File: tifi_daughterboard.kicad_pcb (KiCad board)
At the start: 2 copper layers, 57.4 x 32.3 mm, 19 parts, among them J1 SSW-110-23-F-D, J2 SSW-110-23-F-D, J3 SM04B-SRSS-TB(LF)(SN), J4 SSW-103-02-T-S-RA, Q1 BSS138LT1G, U1 SGP40-D-R4, U2 SHT40-AD1B-R3

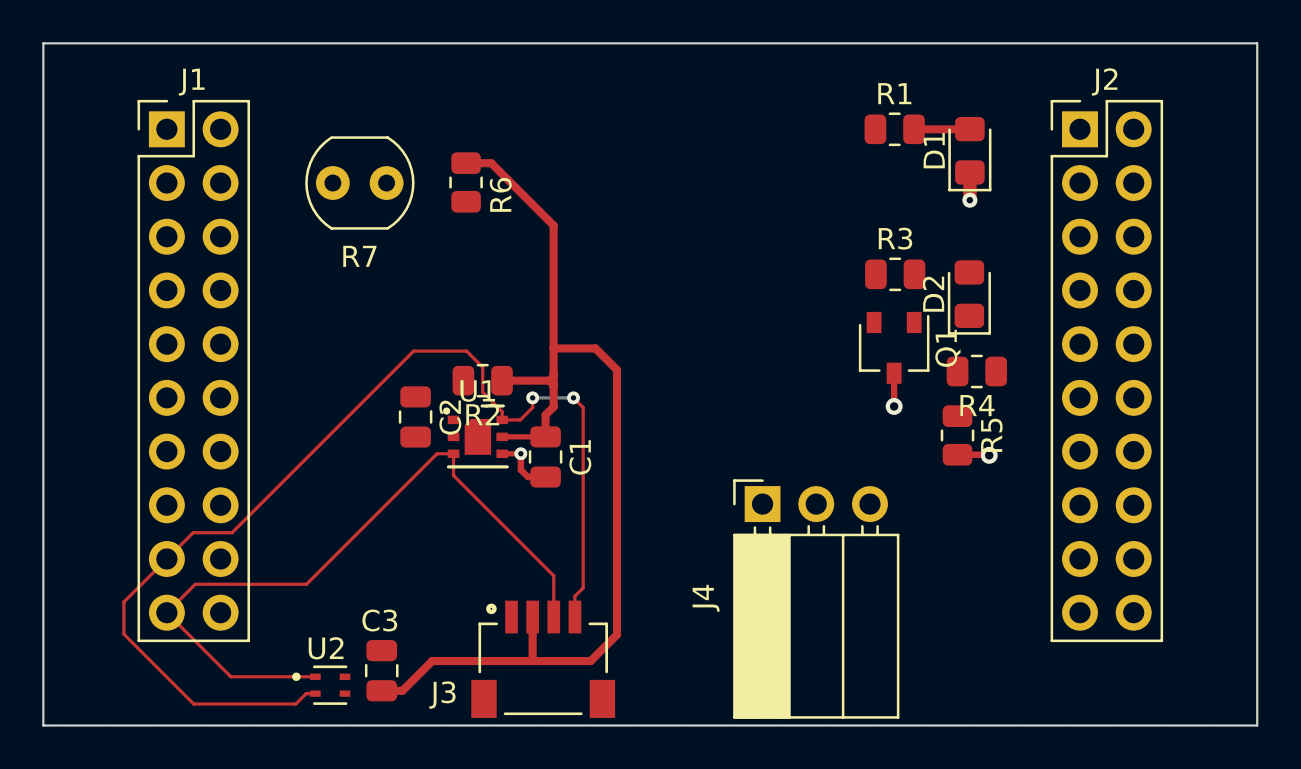
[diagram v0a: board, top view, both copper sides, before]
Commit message: Route 5V rail
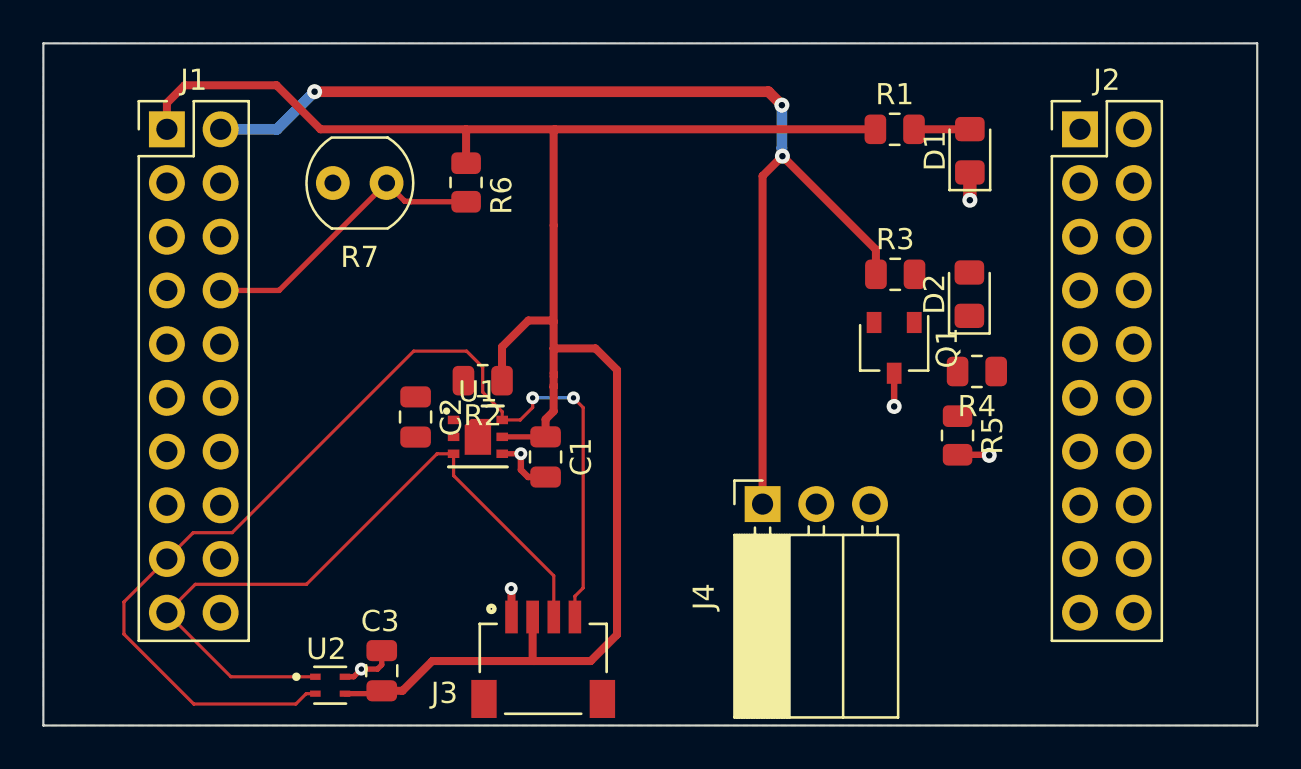
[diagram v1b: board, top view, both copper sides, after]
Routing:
- net +5V: track 0.00 -> 54.2 mm, vias 0 -> 3
- net +3.3V: track 51.0 -> 91.1 mm
- net LDR_OUT: track 0.00 -> 14.1 mm
- net GND: track 7.35 -> 11.3 mm, vias 4 -> 6
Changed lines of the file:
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@@
   (gr_rect (start 116.078 69.596) (end 173.482 101.854) (layer "Edge.Cuts") (width 0.1016) (fill none))
   (segment (start 139.2682 98.806) (end 134.4676 98.806) (width 0.381) (layer "F.Cu") (net 1))
+  (segment (start 140.208 85.852) (end 140.208 86.995) (width 0.381) (layer "F.Cu") (net 1))
+  (segment (start 129.1844 73.66) (end 136.0678 73.66) (width 0.381) (layer "F.Cu") (net 1))
+  (segment (start 137.7677 85.5472) (end 137.7677 83.9489) (width 0.381) (layer "F.Cu") (net 1))
+  (segment (start 140.208 78.2066) (end 140.208 82.7532) (width 0.381) (layer "F.Cu") (net 1))
   (segment (start 141.9606 98.806) (end 139.2682 98.806) (width 0.381) (layer "F.Cu") (net 1))
+  (segment (start 140.208 73.7108) (end 140.2588 73.66) (width 0.381) (layer "F.Cu") (net 1))
+  (segment (start 139.827 87.376) (end 139.827 88.204) (width 0.381) (layer "F.Cu") (net 1))
   (segment (start 139.2682 98.806) (end 139.215 98.7528) (width 0.381) (layer "F.Cu") (net 1))
-  (segment (start 136.0678 75.2621) (end 137.2635 75.2621) (width 0.381) (layer "F.Cu") (net 1))
+  (segment (start 136.0678 75.2621) (end 136.0678 73.66) (width 0.381) (layer "F.Cu") (net 1))
   (segment (start 139.215 98.7528) (end 139.215 96.7232) (width 0.381) (layer "F.Cu") (net 1))
+  (segment (start 139.0142 82.7024) (end 140.1572 82.7024) (width 0.381) (layer "F.Cu") (net 1))
+  (segment (start 136.0678 73.66) (end 140.2588 73.66) (width 0.381) (layer "F.Cu") (net 1))
   (segment (start 143.2052 97.5614) (end 141.9606 98.806) (width 0.381) (layer "F.Cu") (net 1))
   (segment (start 133.0604 100.2132) (end 132.08 100.2132) (width 0.381) (layer "F.Cu") (net 1))
-  (segment (start 140.208 78.2066) (end 140.208 84.0232) (width 0.381) (layer "F.Cu") (net 1))
-  (segment (start 140.208 86.7918) (end 139.827 87.1728) (width 0.381) (layer "F.Cu") (net 1))
+  (segment (start 121.92 72.4154) (end 122.7582 71.5772) (width 0.381) (layer "F.Cu") (net 1))
+  (segment (start 140.2588 73.66) (end 155.4245 73.66) (width 0.381) (layer "F.Cu") (net 1))
   (segment (start 140.208 84.0232) (end 142.1892 84.0232) (width 0.381) (layer "F.Cu") (net 1))
   (segment (start 140.208 85.852) (end 140.208 85.7504) (width 0.381) (layer "F.Cu") (net 1))
-  (segment (start 139.827 87.1728) (end 139.827 88.204) (width 0.381) (layer "F.Cu") (net 1))
+  (segment (start 127.1016 71.5772) (end 129.1844 73.66) (width 0.381) (layer "F.Cu") (net 1))
+  (segment (start 131.9442 100.349) (end 132.08 100.2132) (width 0.254) (layer "F.Cu") (net 1))
   (segment (start 142.1892 84.0232) (end 143.2052 85.0392) (width 0.381) (layer "F.Cu") (net 1))
+  (segment (start 137.7677 83.9489) (end 139.0142 82.7024) (width 0.381) (layer "F.Cu") (net 1))
   (segment (start 140.208 85.344) (end 140.208 85.852) (width 0.381) (layer "F.Cu") (net 1))
   (segment (start 140.208 85.1916) (end 140.208 85.344) (width 0.381) (layer "F.Cu") (net 1))
-  (segment (start 137.2635 75.2621) (end 140.208 78.2066) (width 0.381) (layer "F.Cu") (net 1))
   (segment (start 140.208 84.0232) (end 140.208 85.1916) (width 0.381) (layer "F.Cu") (net 1))
-  (segment (start 140.208 85.344) (end 140.0048 85.5472) (width 0.381) (layer "F.Cu") (net 1))
+  (segment (start 140.208 82.7532) (end 140.208 84.0232) (width 0.381) (layer "F.Cu") (net 1))
+  (segment (start 122.7582 71.5772) (end 127.1016 71.5772) (width 0.381) (layer "F.Cu") (net 1))
+  (segment (start 140.1572 82.7024) (end 140.208 82.7532) (width 0.381) (layer "F.Cu") (net 1))
   (segment (start 143.2052 85.0392) (end 143.2052 97.5614) (width 0.381) (layer "F.Cu") (net 1))
   (segment (start 137.7766 88.204) (end 139.827 88.204) (width 0.254) (layer "F.Cu") (net 1))
-  (segment (start 140.208 85.852) (end 140.208 86.7918) (width 0.381) (layer "F.Cu") (net 1))
-  (segment (start 137.5645 85.5472) (end 140.0048 85.5472) (width 0.381) (layer "F.Cu") (net 1))
+  (segment (start 130.3416 100.349) (end 131.9442 100.349) (width 0.254) (layer "F.Cu") (net 1))
+  (segment (start 140.208 78.2066) (end 140.208 73.7108) (width 0.381) (layer "F.Cu") (net 1))
+  (segment (start 140.208 86.995) (end 139.827 87.376) (width 0.381) (layer "F.Cu") (net 1))
   (segment (start 134.4676 98.806) (end 133.0604 100.2132) (width 0.381) (layer "F.Cu") (net 1))
-  (segment (start 140.208 85.7504) (end 140.0048 85.5472) (width 0.381) (layer "F.Cu") (net 1))
+  (segment (start 121.92 73.66) (end 121.92 72.4154) (width 0.381) (layer "F.Cu") (net 1))
+  (segment (start 138.215 95.4668) (end 138.215 96.7232) (width 0.381) (layer "F.Cu") (net 2))
   (segment (start 137.7766 89.004) (end 138.6562 89.004) (width 0.254) (layer "F.Cu") (net 2))
+  (segment (start 131.1148 99.187) (end 131.8768 99.187) (width 0.254) (layer "F.Cu") (net 2))
   (segment (start 138.6586 89.7636) (end 138.999 90.104) (width 0.3048) (layer "F.Cu") (net 2))
   (segment (start 159.893 77.0128) (end 159.893 75.701) (width 0.635) (layer "F.Cu") (net 2))
   (segment (start 159.3088 89.0505) (end 160.7801 89.0505) (width 0.3048) (layer "F.Cu") (net 2))
+  (segment (start 131.8768 99.187) (end 132.08 98.9838) (width 0.254) (layer "F.Cu") (net 2))
+  (segment (start 138.2014 95.4532) (end 138.215 95.4668) (width 0.381) (layer "F.Cu") (net 2))
   (segment (start 138.6562 89.004) (end 138.6586 89.0016) (width 0.254) (layer "F.Cu") (net 2))
+  (segment (start 130.7528 99.549) (end 131.1148 99.187) (width 0.254) (layer "F.Cu") (net 2))
+  (segment (start 130.3416 99.549) (end 130.7528 99.549) (width 0.254) (layer "F.Cu") (net 2))
   (segment (start 156.3116 85.1959) (end 156.3116 86.7664) (width 0.3048) (layer "F.Cu") (net 2))
   (segment (start 138.999 90.104) (end 139.827 90.104) (width 0.3048) (layer "F.Cu") (net 2))
   (segment (start 160.7801 89.0505) (end 160.8074 89.0778) (width 0.3048) (layer "F.Cu") (net 2))
   (segment (start 138.6586 89.0016) (end 138.6586 89.7636) (width 0.3048) (layer "F.Cu") (net 2))
-  (via (at 160.8074 89.0778) (size 0.8) (drill 0.4) (layers "F.Cu" "B.Cu") (net 2))
+  (segment (start 132.08 98.9838) (end 132.08 98.3132) (width 0.254) (layer "F.Cu") (net 2))
+  (via (at 131.1148 99.187) (size 0.6096) (drill 0.254) (layers "F.Cu" "B.Cu") (free) (net 2))
+  (via (at 160.8074 89.0778) (size 0.7112) (drill 0.3048) (layers "F.Cu" "B.Cu") (net 2))
+  (via (at 138.2014 95.377) (size 0.6096) (drill 0.254) (layers "F.Cu" "B.Cu") (free) (net 2))
   (via (at 138.6586 89.0016) (size 0.6096) (drill 0.254) (layers "F.Cu" "B.Cu") (net 2))
   (via (at 159.893 77.0128) (size 0.7112) (drill 0.3048) (layers "F.Cu" "B.Cu") (free) (net 2))
-  (via (at 156.3116 86.7664) (size 0.8) (drill 0.4) (layers "F.Cu" "B.Cu") (net 2))
+  (via (at 156.3116 86.7664) (size 0.7112) (drill 0.3048) (layers "F.Cu" "B.Cu") (net 2))
   (segment (start 157.2495 73.66) (end 159.884 73.66) (width 0.381) (layer "F.Cu") (net 3))
   (segment (start 159.884 73.66) (end 159.893 73.651) (width 0.381) (layer "F.Cu") (net 3))
+  (segment (start 151.0284 74.93) (end 150.0886 75.8698) (width 0.381) (layer "F.Cu") (net 6))
+  (segment (start 128.905 71.882) (end 150.368 71.882) (width 0.508) (layer "F.Cu") (net 6))
+  (segment (start 150.368 71.882) (end 151.003 72.517) (width 0.508) (layer "F.Cu") (net 6))
+  (segment (start 151.0284 74.93) (end 155.4499 79.3515) (width 0.381) (layer "F.Cu") (net 6))
+  (segment (start 150.0886 75.8698) (end 150.0886 91.3834) (width 0.381) (layer "F.Cu") (net 6))
+  (segment (start 155.4499 79.3515) (end 155.4499 80.518) (width 0.381) (layer "F.Cu") (net 6))
+  (via (at 128.905 71.882) (size 0.7112) (drill 0.3048) (layers "F.Cu" "B.Cu") (net 6))
+  (via (at 151.0284 74.93) (size 0.7112) (drill 0.3048) (layers "F.Cu" "B.Cu") (net 6))
+  (via (at 151.003 72.517) (size 0.7112) (drill 0.3048) (layers "F.Cu" "B.Cu") (net 6))
+  (segment (start 127.127 73.66) (end 128.905 71.882) (width 0.508) (layer "B.Cu") (net 6))
+  (segment (start 124.46 73.66) (end 127.127 73.66) (width 0.508) (layer "B.Cu") (net 6))
+  (segment (start 151.003 74.9046) (end 151.0284 74.93) (width 0.508) (layer "B.Cu") (net 6))
+  (segment (start 151.003 72.517) (end 151.003 74.549) (width 0.508) (layer "B.Cu") (net 6))
+  (segment (start 151.003 74.549) (end 151.003 74.9046) (width 0.508) (layer "B.Cu") (net 6))
+  (segment (start 132.3086 76.2) (end 127.2286 81.28) (width 0.254) (layer "F.Cu") (net 11))
+  (segment (start 136.0678 77.0871) (end 133.4497 77.0871) (width 0.254) (layer "F.Cu") (net 11))
+  (segment (start 133.1722 77.0636) (end 132.3086 76.2) (width 0.254) (layer "F.Cu") (net 11))
+  (segment (start 127.2286 81.28) (end 124.46 81.28) (width 0.254) (layer "F.Cu") (net 11))
+  (segment (start 133.4497 77.0871) (end 133.4262 77.0636) (width 0.254) (layer "F.Cu") (net 11))
+  (segment (start 133.4262 77.0636) (end 133.1722 77.0636) (width 0.254) (layer "F.Cu") (net 11))
   (segment (start 136.0932 84.1502) (end 133.588785 84.1502) (width 0.1524) (layer "F.Cu") (net 20))
   (segment (start 136.8552 86.091359) (end 136.8552 84.9122) (width 0.1524) (layer "F.Cu") (net 20))

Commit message: Route remaining components.
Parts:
- moved D2 6.89 mm to (160.2, 74.6), turned to -90 degrees
- moved R3 6.14 mm to (157.9, 74.6), turned to -90 degrees
- moved Q1 5.98 mm to (159.3, 78.8)
- moved D1 5.72 mm to (154.2, 74.6), turned to -90 degrees
- moved R5 5.33 mm to (158.0, 83.0)
- moved R1 4.34 mm to (152.1, 74.6), turned to -90 degrees
- moved R4 2.13 mm to (160.2, 83.0), turned to 90 degrees
- moved C2 0.56 mm to (133.3, 87.7)
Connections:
- U1 pad 7: (no net) -> GND
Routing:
- net PIR_OUT: track 0.00 -> 45.0 mm
- net LED_PWM: track 0.00 -> 12.6 mm
- net Net-(Q1-Pad2): track 0.00 -> 6.83 mm
- net Net-(D2-Pad1): track 0.00 -> 6.55 mm
- net Net-(C2-Pad1): track 0.00 -> 6.02 mm
- net +3.3V: track 91.1 -> 87.6 mm
- net +5V: track 54.2 -> 56.9 mm, vias 3 -> 1
- net Net-(D2-Pad2): track 0.00 -> 2.33 mm
- net GND: track 11.3 -> 13.1 mm, vias 6 -> 9
- net Net-(D1-Pad2): track 2.65 -> 2.13 mm

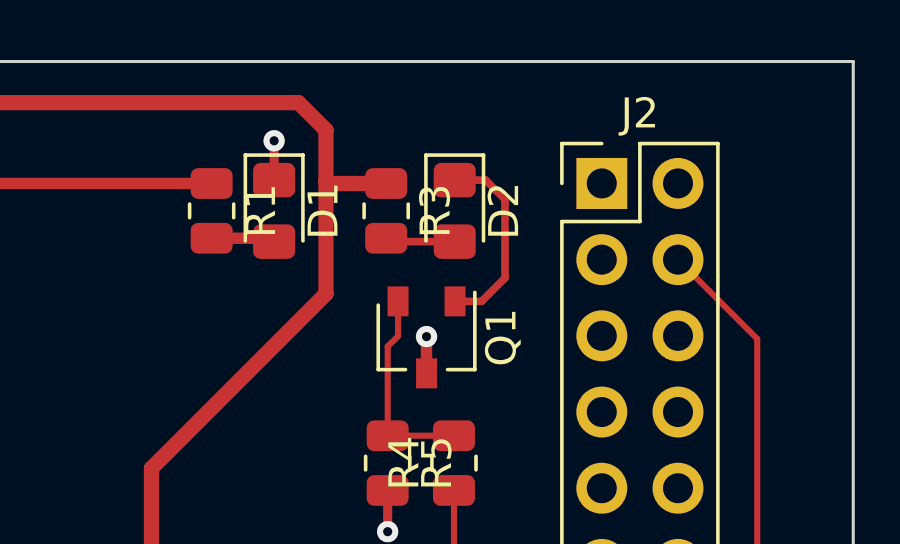
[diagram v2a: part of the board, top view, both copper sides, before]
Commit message: Adjust LED placement.
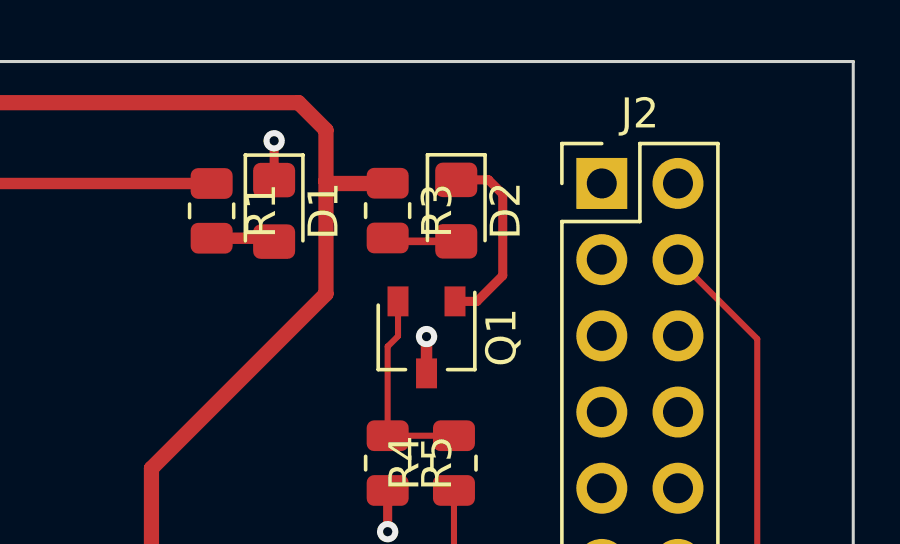
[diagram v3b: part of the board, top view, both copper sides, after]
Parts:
- moved D2 0.05 mm to (160.2, 74.6)
- moved R3 0.05 mm to (158.0, 74.6)
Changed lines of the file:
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@@
   )
   (footprint "LED_SMD:LED_0805_2012Metric_Pad1.15x1.40mm_HandSolder" (layer "F.Cu")
-    (at 160.1978 74.5744 -90)
+    (at 160.2486 74.5654 -90)
     (descr "LED SMD 0805 (2012 Metric), square (rectangular) end terminal, IPC_7351 nominal, (Body size source: https://docs.google.com/spreadsheets/d/1BsfQQcO9C6DZCsRaXUlFlo91Tg2WpOkGARC1WS5S8t0/edit?usp=sharing), generated with kicad-footprint-generator")
     (tags "LED handsolder")
@@
   )
   (footprint "Resistor_SMD:R_0805_2012Metric" (layer "F.Cu")
-    (at 157.9118 74.5744 -90)
+    (at 157.9626 74.5654 -90)
     (descr "Resistor SMD 0805 (2012 Metric), square (rectangular) end terminal, IPC_7351 nominal, (Body size source: IPC-SM-782 page 72, https://www.pcb-3d.com/wordpress/wp-content/uploads/ipc-sm-782a_amendment_1_and_2.pdf), generated with kicad-footprint-generator")
     (tags "resistor")
@@
   (segment (start 154.0655 75.4865) (end 154.178 75.599) (width 0.381) (layer "F.Cu") (net 3))
   (segment (start 152.0952 75.4865) (end 154.0655 75.4865) (width 0.381) (layer "F.Cu") (net 3))
-  (segment (start 160.208 77.5908) (end 161.093 77.5908) (width 0.254) (layer "F.Cu") (net 4))
-  (segment (start 161.2302 73.5494) (end 160.1978 73.5494) (width 0.254) (layer "F.Cu") (net 4))
-  (segment (start 161.8742 74.1934) (end 161.2302 73.5494) (width 0.254) (layer "F.Cu") (net 4))
-  (segment (start 161.8742 76.8096) (end 161.8742 74.1934) (width 0.254) (layer "F.Cu") (net 4))
-  (segment (start 161.093 77.5908) (end 161.8742 76.8096) (width 0.254) (layer "F.Cu") (net 4))
-  (segment (start 158.0243 75.5994) (end 157.9118 75.4869) (width 0.254) (layer "F.Cu") (net 5))
-  (segment (start 160.1978 75.5994) (end 158.0243 75.5994) (width 0.254) (layer "F.Cu") (net 5))
+  (segment (start 161.3228 73.5404) (end 160.2486 73.5404) (width 0.3048) (layer "F.Cu") (net 4))
+  (segment (start 161.798 76.7334) (end 161.798 74.0156) (width 0.3048) (layer "F.Cu") (net 4))
+  (segment (start 160.9406 77.5908) (end 161.798 76.7334) (width 0.3048) (layer "F.Cu") (net 4))
+  (segment (start 161.798 74.0156) (end 161.3228 73.5404) (width 0.3048) (layer "F.Cu") (net 4))
+  (segment (start 160.208 77.5908) (end 160.9406 77.5908) (width 0.3048) (layer "F.Cu") (net 4))
+  (segment (start 158.0751 75.5904) (end 157.9626 75.4779) (width 0.254) (layer "F.Cu") (net 5))
+  (segment (start 160.2486 75.5904) (end 158.0751 75.5904) (width 0.254) (layer "F.Cu") (net 5))
   (segment (start 155.9052 77.343) (end 150.0886 83.1596) (width 0.508) (layer "F.Cu") (net 6))
   (segment (start 150.0886 83.1596) (end 150.0886 91.3834) (width 0.508) (layer "F.Cu") (net 6))
